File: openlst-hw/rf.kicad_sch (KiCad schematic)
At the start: 40 parts, among them J5 ANT, J6 Switch Select, J7 Conn_Coaxial, U3 SF2446E, U4 PE4250MLI, U5 PE4250MLI, U6 0433BM15A0001, U7 RFFM6406

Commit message: RF board BOM
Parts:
- C16, C17, C28, C29, C30, C31: value 1u -> 1uF; Manufactorer YAGEO -> (none); Manufacturer (none) -> Murata; Mfr. # CL10B104KA8NNNC -> (none); Part Number CC0603KRX5R8BB105 -> GRM188R61C105KA12D; Tolerance 10% -> 10
- C18, C21: value 100n -> 100nF; Manufactorer Murata -> (none); Manufacturer (none) -> Murata; Mfr. # GRM32EC81C476KE15L -> (none); Size 1210 -> (none); Tolerance 10% -> 10
- C19, C22: value 10u -> 10uF; Manufactorer Murata -> (none); Manufacturer (none) -> Murata; Mfr. # GRM32EC81C476KE15L -> (none); Part Number GRM21BR61E106KA73L -> GRM188R61E106KA73D; Size 1210 -> (none); Tolerance 10% -> 10
- C20, C23: value 47u -> 47uF; footprint Capacitor_SMD:C_1210_3225Metric_Pad1.33x2.70mm_HandSolder -> Capacitor_SMD:C_1206_3216Metric_Pad1.33x1.80mm_HandSolder; Manufactorer Samsung -> (none); Manufacturer (none) -> Murata; Mfr. # C1608X7S1A475K080AC -> (none); Part Number CL32A476KOJNNNE -> GRM31CR61A476ME15L; Tolerance 10% -> 20; Voltage 15 -> 10
- C24, C38: value 100n -> 100nF; Manufactorer Murata -> (none); Manufacturer (none) -> Murata; Mfr. # CL10B104KA8NNNC -> (none); Tolerance 10% -> 10
- C25: value 100n -> 100nF; Manufactorer Murata -> (none); Manufacturer (none) -> Murata; Mfr. # CL10B105KP8NFNC -> (none); Tolerance 10% -> 10
- C26, C39: value 10u -> 10uF; Manufactorer Murata -> (none); Manufacturer (none) -> Murata; Mfr. # CL10B104KA8NNNC -> (none); Part Number GRM21BR61E106KA73L -> GRM188R61E106KA73D; Tolerance 10% -> 10
- C27: value 47u -> 47uF; footprint Capacitor_SMD:C_1210_3225Metric_Pad1.33x2.70mm_HandSolder -> Capacitor_SMD:C_1206_3216Metric_Pad1.33x1.80mm_HandSolder; Manufactorer Samsung -> (none); Manufacturer (none) -> Murata; Mfr. # CL10B104KA8NNNC -> (none); Part Number CL32A476KOJNNNE -> GRM31CR61A476ME15L; Tolerance 10% -> 20; Voltage 15 -> 10
- C32, C33, C34, C35, C36, C37: value 220p -> 220pF; footprint Capacitor_SMD:C_0603_1608Metric_Pad1.08x0.95mm_HandSolder -> Capacitor_SMD:C_0402_1005Metric_Pad0.74x0.62mm_HandSolder; Manuf Kemet -> (none); ManufPN C0402C221J2GACAUTO -> (none); Manufactorer YAGEO -> (none); Manufacturer (none) -> Murata; Part Number CC0603JRNPO8BN221 -> GRM1555C1H221JA01J; Size 0402 -> (none); Supplier Digikey -> (none); SupplierPN 399-11552-1-ND -> (none); Tolerance 5% -> 5; Voltage 25 -> 50
- FB2, FB3, FB4: value Z=1k @ 100M -> 1K; Manufactorer Murata -> (none); Manufacturer (none) -> Murata; Mfr. # BLM18AG102SN1D -> (none)
- J5: value ANT -> SMA Jack; Manufacturer (none) -> Amphenol; Mfr. # 901-144-8RFX -> (none); Part Number (none) -> 901-144-8RFX
- J6: value Switch Select -> Conn_01x03_Pin
- J7: value Conn_Coaxial -> SMA Jack; Manufacturer (none) -> Amphenol; Mfr. # 901-144-8RFX -> (none); Part Number (none) -> 901-144-8RFX
- R19: footprint Resistor_SMD:R_0603_1608Metric_Pad0.98x0.95mm_HandSolder -> Resistor_SMD:R_0402_1005Metric_Pad0.72x0.64mm_HandSolder; Manufactorer YAGEO -> (none); Manufacturer (none) -> YAGEO; Mfr. # RMCF0603FT3K09 -> (none); Size 0603 -> (none); Tolerance 0.1% -> 0.1
- R20: footprint Resistor_SMD:R_0603_1608Metric_Pad0.98x0.95mm_HandSolder -> Resistor_SMD:R_0402_1005Metric_Pad0.72x0.64mm_HandSolder; Manufactorer YAGEO -> (none); Manufacturer (none) -> YAGEO; Mfr. # RMCF0603FT6K65 -> (none); Size 0603 -> (none); Tolerance 0.1% -> 0.1
- R21: footprint Resistor_SMD:R_0603_1608Metric_Pad0.98x0.95mm_HandSolder -> Resistor_SMD:R_0402_1005Metric_Pad0.72x0.64mm_HandSolder; Manufactorer YAGEO -> (none); Manufacturer (none) -> YAGEO; Mfr. # RMCF0603FT1K00 -> (none); Part Number RT0603BRD0720KL -> RC0402FR-0720KL; Size 0603 -> (none); Tolerance 0.1% -> 1
- R22, R23: footprint Resistor_SMD:R_0603_1608Metric_Pad0.98x0.95mm_HandSolder -> Resistor_SMD:R_0402_1005Metric_Pad0.72x0.64mm_HandSolder; Manufactorer YAGEO -> (none); Manufacturer (none) -> YAGEO; Mfr. # RMCF0603FT1K00 -> (none); Part Number RC0603FR-071KL -> RC0402FR-071KL; Size 0603 -> (none); Tolerance 1% -> 1
- U3: Manufacturer (none) -> RFMi; Mfr. # SF2446E -> (none); Note (none) -> obsolute, last call; Part Number (none) -> SF2446E
- U4, U5: Manuf pSemi -> (none); ManufPN 4259-63 -> (none); Manufacturer (none) -> pSEMI; Mfr. # PE4250MLI-Z -> (none); Part Number (none) -> PE4250MLI-Z; Supplier Digikey -> (none); SupplierPN 1046-1011-1-ND -> (none)
- U6: Manufacturer (none) -> Johannson; Mfr. # 0433BM15A0001E -> (none); Part Number (none) -> 0433BM15A0001001E
- U7: Manuf Qorvo -> (none); ManufPN RFFM6403SB -> (none); Manufacturer (none) -> Quorvo; Note (none) -> obsolete, last call; Part Number (none) -> RFFM6406

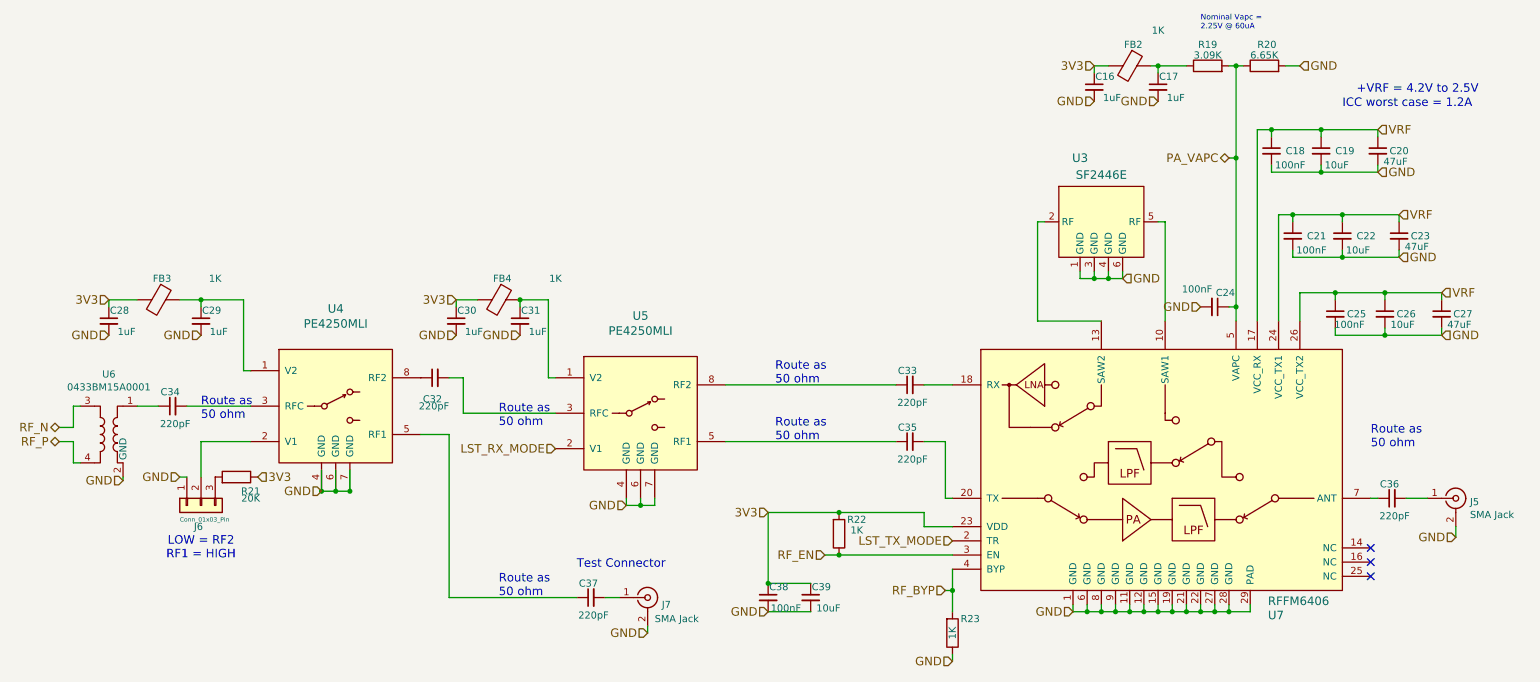
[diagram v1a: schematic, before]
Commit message: add decorations and labels to PCBs
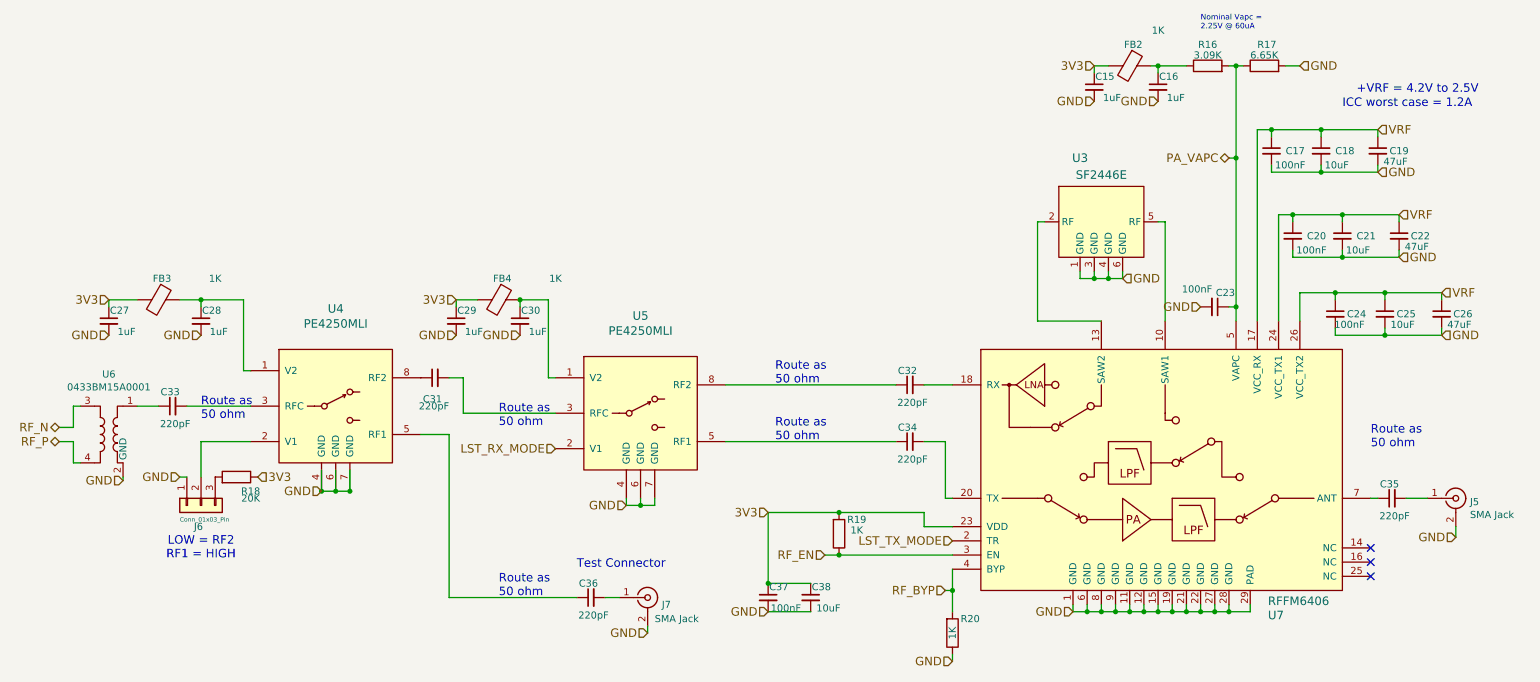
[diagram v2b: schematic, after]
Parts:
- renumbered C16 to C15, C17 to C16, C18 to C17, C19 to C18, C20 to C19, C21 to C20, C22 to C21, C23 to C22, C24 to C23, C25 to C24, C26 to C25, C27 to C26, C28 to C27, C29 to C28, C30 to C29, C31 to C30, C32 to C31, C33 to C32, C34 to C33, C35 to C34, C36 to C35, C37 to C36, C38 to C37, C39 to C38, R19 to R16, R20 to R17, R21 to R18, R22 to R19, R23 to R20
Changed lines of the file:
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@@
 		(on_board yes)
 		(dnp no)
-		(property "Reference" "C39"
+		(property "Reference" "C38"
 			(at 159.385 133.985 0)
 			(effects
@@
 			(project "openlst-hw"
 				(path "/a863a5ec-a5d4-4f54-be53-e8c01d5e3ac4/d6d0e934-53b0-468d-8d79-aec6d2c37df2"
-					(reference "C39")
+					(reference "C38")
 					(unit 1)
 				)
@@
 		(on_board yes)
 		(dnp no)
-		(property "Reference" "C21"
+		(property "Reference" "C20"
 			(at 246.38 71.12 0)
 			(effects
@@
 			(project "openlst-hw"
 				(path "/a863a5ec-a5d4-4f54-be53-e8c01d5e3ac4/d6d0e934-53b0-468d-8d79-aec6d2c37df2"
-					(reference "C21")
+					(reference "C20")
 					(unit 1)
 				)
@@
 		(on_board yes)
 		(dnp no)
-		(property "Reference" "C32"
+		(property "Reference" "C31"
 			(at 91.44 100.33 90)
 			(effects
@@
 			(project "openlst-hw"
 				(path "/a863a5ec-a5d4-4f54-be53-e8c01d5e3ac4/d6d0e934-53b0-468d-8d79-aec6d2c37df2"
-					(reference "C32")
+					(reference "C31")
 					(unit 1)
 				)
@@
 		(on_board yes)
 		(dnp no)
-		(property "Reference" "R22"
+		(property "Reference" "R19"
 			(at 165.735 121.92 0)
 			(effects
@@
 			(project "openlst-hw"
 				(path "/a863a5ec-a5d4-4f54-be53-e8c01d5e3ac4/d6d0e934-53b0-468d-8d79-aec6d2c37df2"
-					(reference "R22")
+					(reference "R19")
 					(unit 1)
 				)
@@
 		(on_board yes)
 		(dnp no)
-		(property "Reference" "C23"
+		(property "Reference" "C22"
 			(at 266.7 71.12 0)
 			(effects
@@
 			(project "openlst-hw"
 				(path "/a863a5ec-a5d4-4f54-be53-e8c01d5e3ac4/d6d0e934-53b0-468d-8d79-aec6d2c37df2"
-					(reference "C23")
+					(reference "C22")
 					(unit 1)
 				)
@@
 		(on_board yes)
 		(dnp no)
-		(property "Reference" "C36"
+		(property "Reference" "C35"
 			(at 262.89 115.57 90)
 			(effects
@@
 			(project "openlst-hw"
 				(path "/a863a5ec-a5d4-4f54-be53-e8c01d5e3ac4/d6d0e934-53b0-468d-8d79-aec6d2c37df2"
-					(reference "C36")
+					(reference "C35")
 					(unit 1)
 				)
@@
 		(on_board yes)
 		(dnp no)
-		(property "Reference" "C33"
+		(property "Reference" "C32"
 			(at 176.53 95.25 90)
 			(effects
@@
 			(project "openlst-hw"
 				(path "/a863a5ec-a5d4-4f54-be53-e8c01d5e3ac4/d6d0e934-53b0-468d-8d79-aec6d2c37df2"
-					(reference "C33")
+					(reference "C32")
 					(unit 1)
 				)
@@
 		(on_board yes)
 		(dnp no)
-		(property "Reference" "C19"
+		(property "Reference" "C18"
 			(at 251.46 55.88 0)
 			(effects
@@
 			(project "openlst-hw"
 				(path "/a863a5ec-a5d4-4f54-be53-e8c01d5e3ac4/d6d0e934-53b0-468d-8d79-aec6d2c37df2"
-					(reference "C19")
+					(reference "C18")
 					(unit 1)
 				)
@@
 		(on_board yes)
 		(dnp no)
-		(property "Reference" "C27"
+		(property "Reference" "C26"
 			(at 274.32 85.09 0)
 			(effects
@@
 			(project "openlst-hw"
 				(path "/a863a5ec-a5d4-4f54-be53-e8c01d5e3ac4/d6d0e934-53b0-468d-8d79-aec6d2c37df2"
-					(reference "C27")
+					(reference "C26")
 					(unit 1)
 				)
@@
 		(on_board yes)
 		(dnp no)
-		(property "Reference" "C37"
+		(property "Reference" "C36"
 			(at 119.38 133.35 90)
 			(effects
@@
 			(project "openlst-hw"
 				(path "/a863a5ec-a5d4-4f54-be53-e8c01d5e3ac4/d6d0e934-53b0-468d-8d79-aec6d2c37df2"
-					(reference "C37")
+					(reference "C36")
 					(unit 1)
 				)
@@
 		(on_board yes)
 		(dnp no)
-		(property "Reference" "C24"
+		(property "Reference" "C23"
 			(at 231.775 81.28 90)
 			(effects
@@
 			(project "openlst-hw"
 				(path "/a863a5ec-a5d4-4f54-be53-e8c01d5e3ac4/d6d0e934-53b0-468d-8d79-aec6d2c37df2"
-					(reference "C24")
+					(reference "C23")
 					(unit 1)
 				)
@@
 		(on_board yes)
 		(dnp no)
-		(property "Reference" "C22"
+		(property "Reference" "C21"
 			(at 255.27 71.12 0)
 			(effects
@@
 			(project "openlst-hw"
 				(path "/a863a5ec-a5d4-4f54-be53-e8c01d5e3ac4/d6d0e934-53b0-468d-8d79-aec6d2c37df2"
-					(reference "C22")
+					(reference "C21")
 					(unit 1)
 				)
@@
 		(on_board yes)
 		(dnp no)
-		(property "Reference" "C18"
+		(property "Reference" "C17"
 			(at 242.57 55.88 0)
 			(effects
@@
 			(project "openlst-hw"
 				(path "/a863a5ec-a5d4-4f54-be53-e8c01d5e3ac4/d6d0e934-53b0-468d-8d79-aec6d2c37df2"
-					(reference "C18")
+					(reference "C17")
 					(unit 1)
 				)
@@
 		(on_board yes)
 		(dnp no)
-		(property "Reference" "R21"
+		(property "Reference" "R18"
 			(at 57.15 116.84 90)
 			(effects
@@
 			(project "openlst-hw"
 				(path "/a863a5ec-a5d4-4f54-be53-e8c01d5e3ac4/d6d0e934-53b0-468d-8d79-aec6d2c37df2"
-					(reference "R21")
+					(reference "R18")
 					(unit 1)
 				)
@@
 		(on_board yes)
 		(dnp no)
-		(property "Reference" "C16"
+		(property "Reference" "C15"
 			(at 210.185 42.545 0)
 			(effects
@@
 			(project "openlst-hw"
 				(path "/a863a5ec-a5d4-4f54-be53-e8c01d5e3ac4/d6d0e934-53b0-468d-8d79-aec6d2c37df2"
-					(reference "C16")
+					(reference "C15")
 					(unit 1)
 				)
@@
 		(on_board yes)
 		(dnp no)
-		(property "Reference" "C29"
+		(property "Reference" "C28"
 			(at 50.165 84.455 0)
 			(effects
@@
 			(project "openlst-hw"
 				(path "/a863a5ec-a5d4-4f54-be53-e8c01d5e3ac4/d6d0e934-53b0-468d-8d79-aec6d2c37df2"
-					(reference "C29")
+					(reference "C28")
 					(unit 1)
 				)
@@
 		(on_board yes)
 		(dnp no)
-		(property "Reference" "C26"
+		(property "Reference" "C25"
 			(at 264.16 85.09 0)
 			(effects
@@
 			(project "openlst-hw"
 				(path "/a863a5ec-a5d4-4f54-be53-e8c01d5e3ac4/d6d0e934-53b0-468d-8d79-aec6d2c37df2"
-					(reference "C26")
+					(reference "C25")
 					(unit 1)
 				)
@@
 		(on_board yes)
 		(dnp no)
-		(property "Reference" "C30"
+		(property "Reference" "C29"
 			(at 95.885 84.455 0)
 			(effects
@@
 			(project "openlst-hw"
 				(path "/a863a5ec-a5d4-4f54-be53-e8c01d5e3ac4/d6d0e934-53b0-468d-8d79-aec6d2c37df2"
-					(reference "C30")
+					(reference "C29")
 					(unit 1)
 				)
@@
 		(on_board yes)
 		(dnp no)
-		(property "Reference" "C35"
+		(property "Reference" "C34"
 			(at 176.53 105.41 90)
 			(effects
@@
 			(project "openlst-hw"
 				(path "/a863a5ec-a5d4-4f54-be53-e8c01d5e3ac4/d6d0e934-53b0-468d-8d79-aec6d2c37df2"
-					(reference "C35")
+					(reference "C34")
 					(unit 1)
 				)
@@
 		(on_board yes)
 		(dnp no)
-		(property "Reference" "C34"
+		(property "Reference" "C33"
 			(at 44.45 99.06 90)
 			(effects
@@
 			(project "openlst-hw"
 				(path "/a863a5ec-a5d4-4f54-be53-e8c01d5e3ac4/d6d0e934-53b0-468d-8d79-aec6d2c37df2"
-					(reference "C34")
+					(reference "C33")
 					(unit 1)
 				)
@@
 		(on_board yes)
 		(dnp no)
-		(property "Reference" "R20"
+		(property "Reference" "R17"
 			(at 237.49 36.83 90)
 			(effects
@@
 			(project "openlst-hw"
 				(path "/a863a5ec-a5d4-4f54-be53-e8c01d5e3ac4/d6d0e934-53b0-468d-8d79-aec6d2c37df2"
-					(reference "R20")
+					(reference "R17")
 					(unit 1)
 				)
@@
 		(on_board yes)
 		(dnp no)
-		(property "Reference" "C28"
+		(property "Reference" "C27"
 			(at 33.655 84.455 0)
 			(effects
@@
 			(project "openlst-hw"
 				(path "/a863a5ec-a5d4-4f54-be53-e8c01d5e3ac4/d6d0e934-53b0-468d-8d79-aec6d2c37df2"
-					(reference "C28")
+					(reference "C27")
 					(unit 1)
 				)
@@
 		(on_board yes)
 		(dnp no)
-		(property "Reference" "C38"
+		(property "Reference" "C37"
 			(at 151.765 133.985 0)
 			(effects
@@
 			(project "openlst-hw"
 				(path "/a863a5ec-a5d4-4f54-be53-e8c01d5e3ac4/d6d0e934-53b0-468d-8d79-aec6d2c37df2"
-					(reference "C38")
+					(reference "C37")
 					(unit 1)
 				)
@@
 		(on_board yes)
 		(dnp no)
-		(property "Reference" "R23"
+		(property "Reference" "R20"
 			(at 186.055 139.7 0)
 			(effects
@@
 			(project "openlst-hw"
 				(path "/a863a5ec-a5d4-4f54-be53-e8c01d5e3ac4/d6d0e934-53b0-468d-8d79-aec6d2c37df2"
-					(reference "R23")
+					(reference "R20")
 					(unit 1)
 				)
@@
 		(on_board yes)
 		(dnp no)
-		(property "Reference" "C31"
+		(property "Reference" "C30"
 			(at 107.315 84.455 0)
 			(effects
@@
 			(project "openlst-hw"
 				(path "/a863a5ec-a5d4-4f54-be53-e8c01d5e3ac4/d6d0e934-53b0-468d-8d79-aec6d2c37df2"
-					(reference "C31")
+					(reference "C30")
 					(unit 1)
 				)
@@
 		(on_board yes)
 		(dnp no)
-		(property "Reference" "R19"
+		(property "Reference" "R16"
 			(at 228.6 36.83 90)
 			(effects
@@
 			(project "openlst-hw"
 				(path "/a863a5ec-a5d4-4f54-be53-e8c01d5e3ac4/d6d0e934-53b0-468d-8d79-aec6d2c37df2"
-					(reference "R19")
+					(reference "R16")
 					(unit 1)
 				)
@@
 		(on_board yes)
 		(dnp no)
-		(property "Reference" "C25"
+		(property "Reference" "C24"
 			(at 255.27 85.09 0)
 			(effects
@@
 			(project "openlst-hw"
 				(path "/a863a5ec-a5d4-4f54-be53-e8c01d5e3ac4/d6d0e934-53b0-468d-8d79-aec6d2c37df2"
-					(reference "C25")
+					(reference "C24")
 					(unit 1)
 				)
@@
 		(on_board yes)
 		(dnp no)
-		(property "Reference" "C20"
+		(property "Reference" "C19"
 			(at 262.89 55.88 0)
 			(effects
@@
 			(project "openlst-hw"
 				(path "/a863a5ec-a5d4-4f54-be53-e8c01d5e3ac4/d6d0e934-53b0-468d-8d79-aec6d2c37df2"
-					(reference "C20")
+					(reference "C19")
 					(unit 1)
 				)
@@
 		(on_board yes)
 		(dnp no)
-		(property "Reference" "C17"
+		(property "Reference" "C16"
 			(at 221.615 42.545 0)
 			(effects
@@
 			(project "openlst-hw"
 				(path "/a863a5ec-a5d4-4f54-be53-e8c01d5e3ac4/d6d0e934-53b0-468d-8d79-aec6d2c37df2"
-					(reference "C17")
+					(reference "C16")
 					(unit 1)
 				)

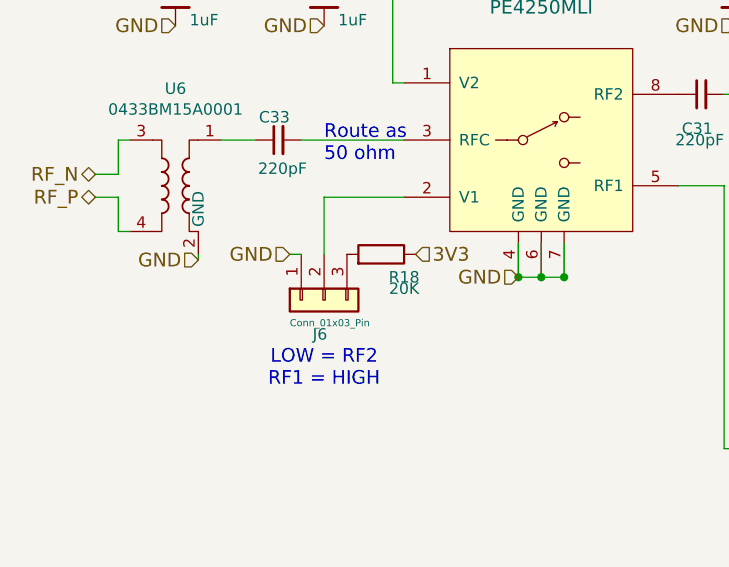
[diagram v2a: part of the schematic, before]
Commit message: add decorations and labels to PCBs part 2
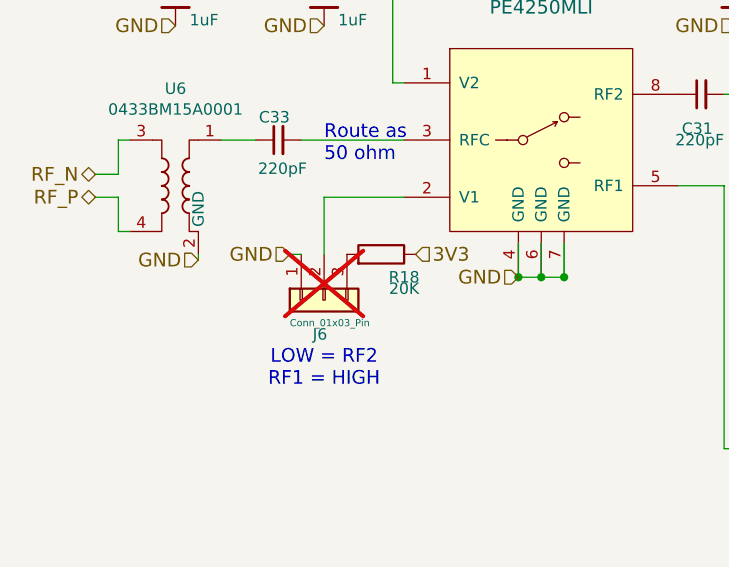
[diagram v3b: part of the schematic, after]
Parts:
- J6: now not fitted
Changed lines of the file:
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@@
 		(in_bom yes)
 		(on_board yes)
-		(dnp no)
+		(dnp yes)
 		(property "Reference" "J6"
 			(at 46.99 123.19 90)
